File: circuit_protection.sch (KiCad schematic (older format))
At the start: 12 parts, among them J1 +VIN, J2 -VIN, J3 +VOUT, J4 -VOUT, Q1 DMP4065S, Q2 DMP4065S, Q3 PMBT2907A

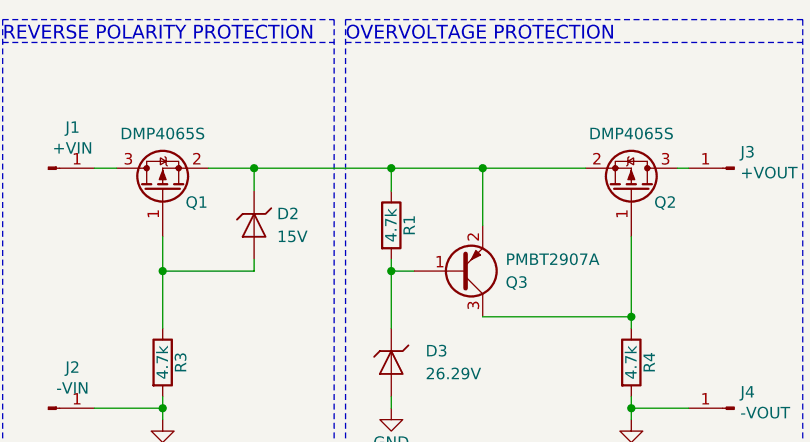
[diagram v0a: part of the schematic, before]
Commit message: label node A on schematic
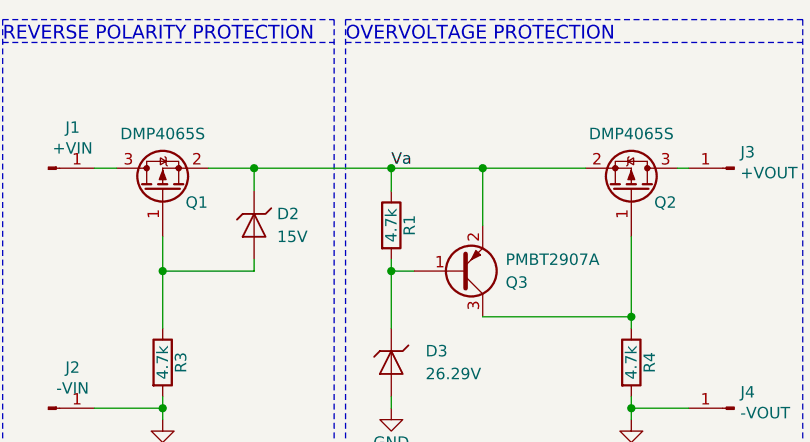
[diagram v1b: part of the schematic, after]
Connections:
- net Va: now reaches D2.1 (K), Q1.2 (S), Q2.2 (S), Q3.2 (E), R1.1
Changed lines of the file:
@@
 EESchema Schematic File Version 4
+LIBS:circuit_protection-cache
 EELAYER 26 0
 EELAYER END
@@
 Wire Wire Line
 	5700 4300 5700 4250
+Text Label 4650 3250 0    50   ~ 0
+Va
 $EndSCHEMATC

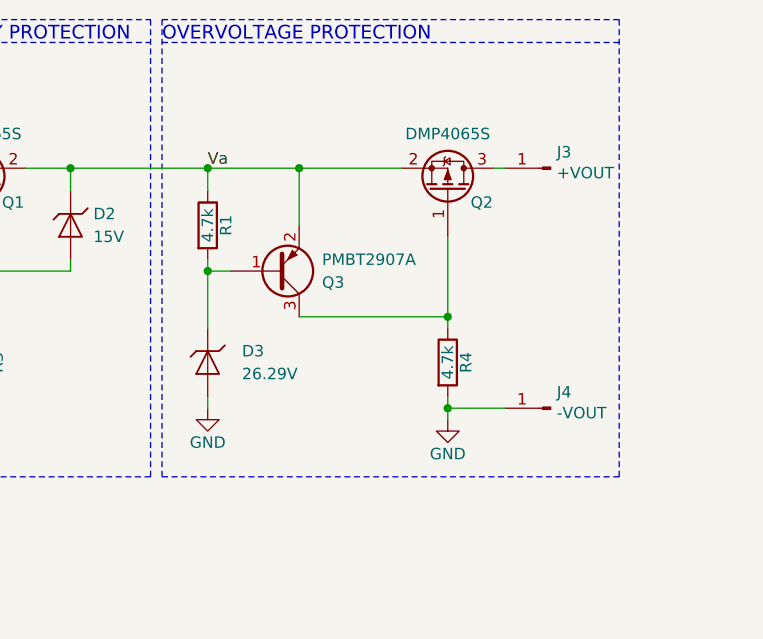
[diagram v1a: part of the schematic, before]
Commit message: add zener to limit gate voltage of Q2
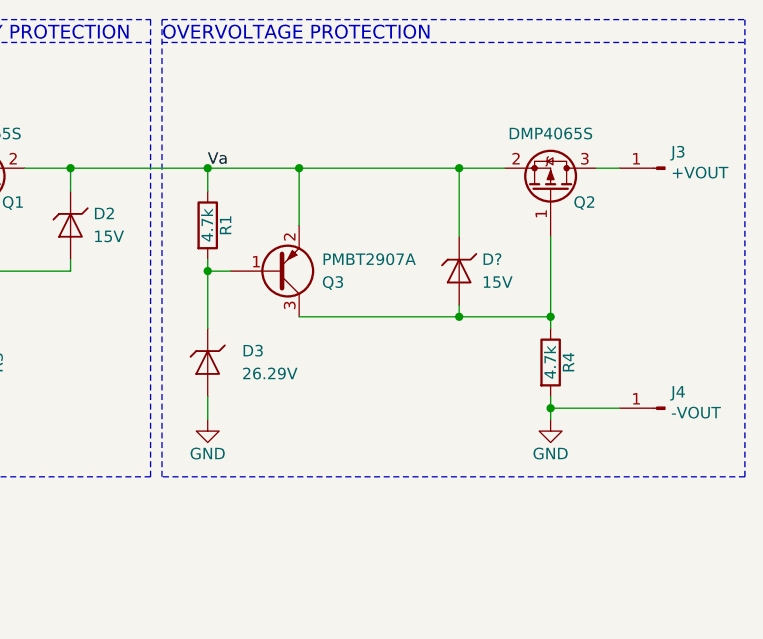
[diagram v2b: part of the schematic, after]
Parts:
- added D?: 15V, Vishay:Vishay_TZM5258B_SOD80, symbol Vishay:D_Zener
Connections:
- net Va: now also D?.1 (K)
- net at Q2.1 (G), Q3.3 (C), R4.1: now also D?.2 (A)
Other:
- moved on the sheet: J3, J4, Q2, R4
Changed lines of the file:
@@
 L Device:Q_PMOS_GSD Q2
 U 1 1 5C1AB09D
-P 5700 3350
-F 0 "Q2" V 5650 3450 50  0000 L CNN
-F 1 "DMP4065S" V 5950 3350 50  0000 C CNN
-F 2 "Package_TO_SOT_SMD:SOT-23" H 5900 3450 50  0001 C CNN
-F 3 "https://www.diodes.com/assets/Datasheets/DMP4065S.pdf" H 5700 3350 50  0001 C CNN
-F 4 "Diodes Incorporated" H 5700 3350 50  0001 C CNN "Manufacture"
-F 5 "DMP4065S" H 5700 3350 50  0001 C CNN "Mfg Part Number"
-F 6 "MOSFET P-CH 40V 2.4A SOT23" H 5700 3350 50  0001 C CNN "Description"
-F 7 "Digi-Key" H 5700 3350 50  0001 C CNN "Supplier"
-F 8 "DMP4065S-7DICT-ND" H 5700 3350 50  0001 C CNN "Supplier PN"
-	1    5700 3350
+P 6150 3350
+F 0 "Q2" V 6100 3450 50  0000 L CNN
+F 1 "DMP4065S" V 6400 3350 50  0000 C CNN
+F 2 "Package_TO_SOT_SMD:SOT-23" H 6350 3450 50  0001 C CNN
+F 3 "https://www.diodes.com/assets/Datasheets/DMP4065S.pdf" H 6150 3350 50  0001 C CNN
+F 4 "Diodes Incorporated" H 6150 3350 50  0001 C CNN "Manufacture"
+F 5 "DMP4065S" H 6150 3350 50  0001 C CNN "Mfg Part Number"
+F 6 "MOSFET P-CH 40V 2.4A SOT23" H 6150 3350 50  0001 C CNN "Description"
+F 7 "Digi-Key" H 6150 3350 50  0001 C CNN "Supplier"
+F 8 "DMP4065S-7DICT-ND" H 6150 3350 50  0001 C CNN "Supplier PN"
+	1    6150 3350
 	0    1    -1   0
 $EndComp
@@
 L Device:R R4
 U 1 1 5C1AD166
-P 5700 4100
-F 0 "R4" V 5780 4100 50  0000 C CNN
-F 1 "4.7k" V 5700 4100 50  0000 C CNN
-F 2 "Resistor_THT:R_Axial_DIN0207_L6.3mm_D2.5mm_P10.16mm_Horizontal" V 5630 4100 50  0001 C CNN
-F 3 "~" H 5700 4100 50  0001 C CNN
-	1    5700 4100
+P 6150 4100
+F 0 "R4" V 6230 4100 50  0000 C CNN
+F 1 "4.7k" V 6150 4100 50  0000 C CNN
+F 2 "Resistor_THT:R_Axial_DIN0207_L6.3mm_D2.5mm_P10.16mm_Horizontal" V 6080 4100 50  0001 C CNN
+F 3 "~" H 6150 4100 50  0001 C CNN
+	1    6150 4100
 	1    0    0    -1
 $EndComp
@@
 	4650 3250 5050 3250
 Wire Wire Line
-	5700 3950 5700 3900
-Wire Wire Line
-	5050 3900 5700 3900
-Connection ~ 5700 3900
-Wire Wire Line
-	5700 3900 5700 3550
+	6150 3950 6150 3900
+Wire Wire Line
+	5050 3900 5750 3900
+Connection ~ 6150 3900
+Wire Wire Line
+	6150 3900 6150 3550
 Wire Wire Line
 	5050 3500 5050 3250
 Connection ~ 5050 3250
 Wire Wire Line
-	5050 3250 5500 3250
+	5050 3250 5750 3250
 $Comp
 L power:GND #PWR04
 U 1 1 5C1B3816
-P 4650 4300
-F 0 "#PWR04" H 4650 4050 50  0001 C CNN
-F 1 "GND" H 4650 4150 50  0000 C CNN
-F 2 "" H 4650 4300 50  0001 C CNN
-F 3 "" H 4650 4300 50  0001 C CNN
-	1    4650 4300
+P 4650 4350
+F 0 "#PWR04" H 4650 4100 50  0001 C CNN
+F 1 "GND" H 4650 4200 50  0000 C CNN
+F 2 "" H 4650 4350 50  0001 C CNN
+F 3 "" H 4650 4350 50  0001 C CNN
+	1    4650 4350
 	1    0    0    -1
 $EndComp
@@
 L power:GND #PWR05
 U 1 1 5C1B384E
-P 5700 4350
-F 0 "#PWR05" H 5700 4100 50  0001 C CNN
-F 1 "GND" H 5700 4200 50  0000 C CNN
-F 2 "" H 5700 4350 50  0001 C CNN
-F 3 "" H 5700 4350 50  0001 C CNN
-	1    5700 4350
-	1    0    0    -1
-$EndComp
-Wire Wire Line
-	5700 4350 5700 4300
-Wire Wire Line
-	4650 4300 4650 4250
+P 6150 4350
+F 0 "#PWR05" H 6150 4100 50  0001 C CNN
+F 1 "GND" H 6150 4200 50  0000 C CNN
+F 2 "" H 6150 4350 50  0001 C CNN
+F 3 "" H 6150 4350 50  0001 C CNN
+	1    6150 4350
+	1    0    0    -1
+$EndComp
+Wire Wire Line
+	6150 4350 6150 4300
+Wire Wire Line
+	4650 4350 4650 4250
 Wire Wire Line
 	4650 3250 4050 3250
@@
 OVERVOLTAGE PROTECTION
 Wire Notes Line
-	4450 2600 6450 2600
-Wire Notes Line
-	6450 2600 6450 4600
-Wire Notes Line
-	6450 4600 4450 4600
+	4450 2600 7000 2600
+Wire Notes Line
+	7000 2600 7000 4600
+Wire Notes Line
+	7000 4600 4450 4600
 Wire Notes Line
 	4450 4600 4450 2600
 Wire Notes Line
-	4450 2700 6450 2700
+	4450 2700 7000 2700
 Text Notes 2950 2700 0    60   ~ 0
 REVERSE POLARITY PROTECTION
@@
 L Connector:Conn_01x01_Male J3
 U 1 1 5C288863
-P 6150 3250
-F 0 "J3" H 6123 3180 50  0000 R CNN
-F 1 "+VOUT" H 6123 3271 50  0000 R CNN
-F 2 "TestPoint:TestPoint_THTPad_D1.5mm_Drill0.7mm" H 6150 3250 50  0001 C CNN
-F 3 "~" H 6150 3250 50  0001 C CNN
-	1    6150 3250
+P 6650 3250
+F 0 "J3" H 6623 3180 50  0000 R CNN
+F 1 "+VOUT" H 6623 3271 50  0000 R CNN
+F 2 "TestPoint:TestPoint_THTPad_D1.5mm_Drill0.7mm" H 6650 3250 50  0001 C CNN
+F 3 "~" H 6650 3250 50  0001 C CNN
+	1    6650 3250
 	-1   0    0    1
 $EndComp
 Wire Wire Line
-	5900 3250 5950 3250
+	6350 3250 6450 3250
 $Comp
 L Connector:Conn_01x01_Male J2
@@
 L Connector:Conn_01x01_Male J4
 U 1 1 5C28A4F0
-P 6150 4300
-F 0 "J4" H 6123 4230 50  0000 R CNN
-F 1 "-VOUT" H 6123 4321 50  0000 R CNN
-F 2 "TestPoint:TestPoint_THTPad_D1.5mm_Drill0.7mm" H 6150 4300 50  0001 C CNN
-F 3 "~" H 6150 4300 50  0001 C CNN
-	1    6150 4300
+P 6650 4300
+F 0 "J4" H 6623 4230 50  0000 R CNN
+F 1 "-VOUT" H 6623 4321 50  0000 R CNN
+F 2 "TestPoint:TestPoint_THTPad_D1.5mm_Drill0.7mm" H 6650 4300 50  0001 C CNN
+F 3 "~" H 6650 4300 50  0001 C CNN
+	1    6650 4300
 	-1   0    0    1
 $EndComp
 Wire Wire Line
-	5950 4300 5700 4300
-Connection ~ 5700 4300
-Wire Wire Line
-	5700 4300 5700 4250
+	6450 4300 6150 4300
+Connection ~ 6150 4300
+Wire Wire Line
+	6150 4300 6150 4250
 Text Label 4650 3250 0    50   ~ 0
 Va
+$Comp
+L Vishay:D_Zener D?
+U 1 1 5C2ACD9F
+P 5750 3700
+F 0 "D?" V 5700 3800 50  0000 L CNN
+F 1 "15V" V 5800 3800 50  0000 L CNN
+F 2 "Vishay:Vishay_TZM5258B_SOD80" H 5750 3700 50  0001 C CNN
+F 3 "http://www.vishay.com/docs/85635/tlz.pdf" H 5750 3700 50  0001 C CNN
+F 4 "Vishay Semiconductor Diodes Division" H 5750 3700 50  0001 C CNN "Manufacture"
+F 5 "TLZ15A-GS08" H 5750 3700 50  0001 C CNN "Mfg Part Number"
+F 6 "DIODE ZENER 15V 500MW SOD80" H 5750 3700 50  0001 C CNN "Description"
+F 7 "Digi-Key" H 5750 3700 50  0001 C CNN "Supplier"
+F 8 "TLZ15A-GS08GICT-ND" H 5750 3700 50  0001 C CNN "Supplier PN"
+	1    5750 3700
+	0    1    1    0
+$EndComp
+Wire Wire Line
+	5750 3900 5750 3850
+Connection ~ 5750 3900
+Wire Wire Line
+	5750 3900 6150 3900
+Wire Wire Line
+	5750 3550 5750 3250
+Connection ~ 5750 3250
+Wire Wire Line
+	5750 3250 5950 3250
 $EndSCHEMATC

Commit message: annotate new zener
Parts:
- gave numbers to parts that had none: 1
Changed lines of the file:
@@
 Va
 $Comp
-L Vishay:D_Zener D?
+L Vishay:D_Zener D1
 U 1 1 5C2ACD9F
 P 5750 3700
-F 0 "D?" V 5700 3800 50  0000 L CNN
+F 0 "D1" V 5700 3800 50  0000 L CNN
 F 1 "15V" V 5800 3800 50  0000 L CNN
 F 2 "Vishay:Vishay_TZM5258B_SOD80" H 5750 3700 50  0001 C CNN
